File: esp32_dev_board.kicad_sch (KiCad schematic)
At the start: 27 parts, among them J1 USB_B_Micro, J2 Conn_01x12, J3 Conn_01x12, Q1 Q_PMOS_GSD, Q2 MBT3904DW1, SW1 SW_Push, U1 ESP32-WROOM-32, U2 AP2112K-3.3, U3 FT231XS

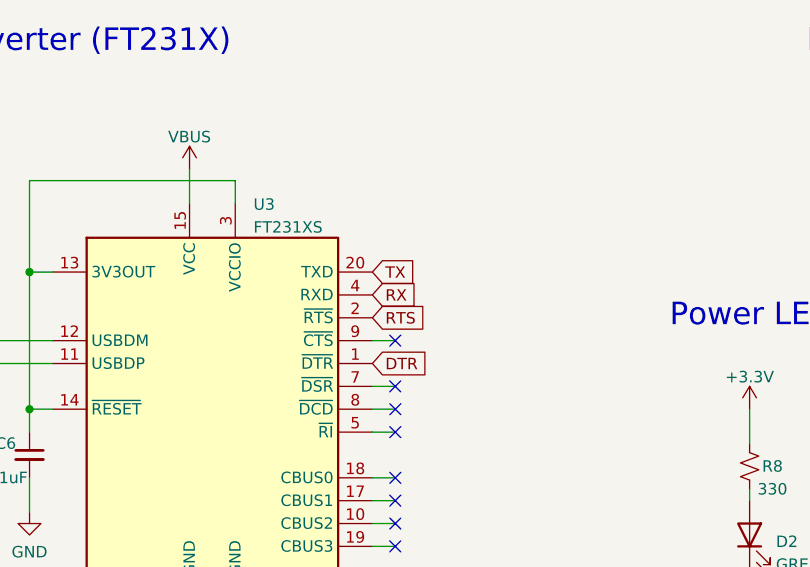
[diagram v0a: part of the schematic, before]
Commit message: Change global labels TX and RX to TX0 and RX0
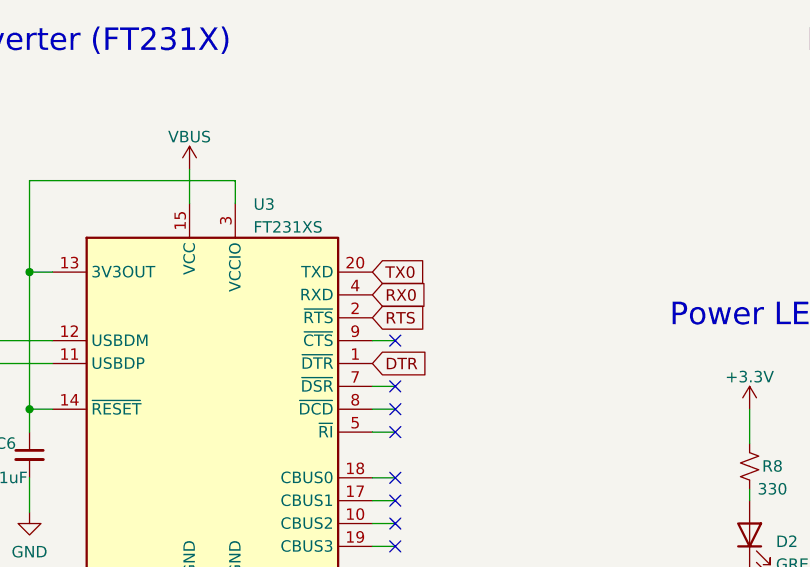
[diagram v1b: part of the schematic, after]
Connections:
- net RX is gone; now on net RX0: U3.4 (RXD)
- net TX is gone; now on net TX0: U3.20 (TXD)
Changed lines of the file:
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@@
     )
   )
-  (global_label "RX" (shape input) (at 181.61 55.88 0) (fields_autoplaced)
+  (global_label "RX0" (shape input) (at 181.61 55.88 0) (fields_autoplaced)
     (effects (font (size 1.27 1.27)) (justify left))
-    (property "Intersheet References" "${INTERSHEET_REFS}" (id 0) (at 186.5026 55.8006 0)
+    (property "Intersheet References" "${INTERSHEET_REFS}" (id 0) (at 187.7121 55.8006 0)
       (effects (font (size 1.27 1.27)) (justify left) hide)
     )
@@
     )
   )
-  (global_label "TX" (shape input) (at 181.61 53.34 0) (fields_autoplaced)
+  (global_label "TX0" (shape input) (at 181.61 53.34 0) (fields_autoplaced)
     (effects (font (size 1.27 1.27)) (justify left))
-    (property "Intersheet References" "${INTERSHEET_REFS}" (id 0) (at 186.2002 53.2606 0)
+    (property "Intersheet References" "${INTERSHEET_REFS}" (id 0) (at 187.4098 53.2606 0)
       (effects (font (size 1.27 1.27)) (justify left) hide)
     )

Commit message: Add silkscreen, round corners, and small fixes
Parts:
- added C7: 1uF, Capacitor_SMD:C_0805_2012Metric_Pad1.18x1.45mm_HandSolder, symbol Device:C_Small
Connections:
- net GND: now also C7.2
- net VIN: now also C7.1
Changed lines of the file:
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@@
   (junction (at 151.13 162.56) (diameter 0) (color 0 0 0 0)
+  )
+  (junction (at 44.45 149.86) (diameter 0) (color 0 0 0 0)
   )
   (no_connect (at 71.12 54.61))
@@
   (no_connect (at 33.02 92.71))
   (no_connect (at 33.02 90.17))
+  (wire (pts (xy 68.58 52.07) (xy 67.31 52.07))
+    (stroke (width 0) (type default) (color 0 0 0 0))
+  )
   (wire (pts (xy 233.68 39.37) (xy 233.68 43.18))
     (stroke (width 0) (type default) (color 0 0 0 0))
@@
     (stroke (width 0) (type default) (color 0 0 0 0))
   )
+  (wire (pts (xy 21.59 176.53) (xy 21.59 180.34))
+    (stroke (width 0) (type default) (color 0 0 0 0))
+  )
   (wire (pts (xy 33.02 85.09) (xy 36.83 85.09))
     (stroke (width 0) (type default) (color 0 0 0 0))
@@
     (stroke (width 0) (type default) (color 0 0 0 0))
   )
-  (wire (pts (xy 29.21 149.86) (xy 29.21 158.75))
+  (wire (pts (xy 29.21 156.21) (xy 29.21 158.75))
     (stroke (width 0) (type default) (color 0 0 0 0))
   )
@@
     (stroke (width 0) (type default) (color 0 0 0 0))
   )
+  (wire (pts (xy 21.59 149.86) (xy 44.45 149.86))
+    (stroke (width 0) (type default) (color 0 0 0 0))
+  )
   (wire (pts (xy 44.45 168.91) (xy 58.42 168.91))
     (stroke (width 0) (type default) (color 0 0 0 0))
@@
     (stroke (width 0) (type default) (color 0 0 0 0))
   )
+  (wire (pts (xy 68.58 49.53) (xy 67.31 49.53))
+    (stroke (width 0) (type default) (color 0 0 0 0))
+  )
   (wire (pts (xy 151.13 172.72) (xy 151.13 162.56))
     (stroke (width 0) (type default) (color 0 0 0 0))
@@
   )
   (wire (pts (xy 138.43 63.5) (xy 146.05 63.5))
+    (stroke (width 0) (type default) (color 0 0 0 0))
+  )
+  (wire (pts (xy 21.59 171.45) (xy 21.59 149.86))
     (stroke (width 0) (type default) (color 0 0 0 0))
   )
@@
     )
   )
-  (global_label "GPIO0" (shape input) (at 67.31 49.53 0) (fields_autoplaced)
-    (effects (font (size 1.27 1.27)) (justify left))
-    (property "Intersheet References" "${INTERSHEET_REFS}" (id 0) (at 75.4079 49.4506 0)
+  (global_label "GPIO0" (shape input) (at 68.58 49.53 0) (fields_autoplaced)
+    (effects (font (size 1.27 1.27)) (justify left))
+    (property "Intersheet References" "${INTERSHEET_REFS}" (id 0) (at 76.6779 49.4506 0)
       (effects (font (size 1.27 1.27)) (justify left) hide)
     )
@@
     )
   )
-  (global_label "TX0" (shape input) (at 67.31 52.07 0) (fields_autoplaced)
-    (effects (font (size 1.27 1.27)) (justify left))
-    (property "Intersheet References" "${INTERSHEET_REFS}" (id 0) (at 73.1098 51.9906 0)
+  (global_label "TX0" (shape input) (at 68.58 52.07 0) (fields_autoplaced)
+    (effects (font (size 1.27 1.27)) (justify left))
+    (property "Intersheet References" "${INTERSHEET_REFS}" (id 0) (at 74.3798 51.9906 0)
       (effects (font (size 1.27 1.27)) (justify left) hide)
     )
@@
     )
     (property "Datasheet" "" (id 3) (at 270.51 156.21 0)
+      (effects (font (size 1.27 1.27)) hide)
+    )
+    (pin "1")
+  )
+  (symbol (lib_id "power:GND") (at 21.59 180.34 0) (unit 1)
+    (in_bom yes) (on_board yes) (fields_autoplaced)
+    (property "Reference" "#PWR024" (id 0) (at 21.59 186.69 0)
+      (effects (font (size 1.27 1.27)) hide)
+    )
+    (property "Value" "GND" (id 1) (at 21.59 184.7834 0))
+    (property "Footprint" "" (id 2) (at 21.59 180.34 0)
+      (effects (font (size 1.27 1.27)) hide)
+    )
+    (property "Datasheet" "" (id 3) (at 21.59 180.34 0)
       (effects (font (size 1.27 1.27)) hide)
     )
@@
     (pin "2")
   )
+  (symbol (lib_id "Device:C_Small") (at 21.59 173.99 0) (unit 1)
+    (in_bom yes) (on_board yes)
+    (property "Reference" "C7" (id 0) (at 16.51 175.26 0)
+      (effects (font (size 1.27 1.27)) (justify left))
+    )
+    (property "Value" "1uF" (id 1) (at 16.51 177.8 0)
+      (effects (font (size 1.27 1.27)) (justify left))
+    )
+    (property "Footprint" "Capacitor_SMD:C_0805_2012Metric_Pad1.18x1.45mm_HandSolder" (id 2) (at 21.59 173.99 0)
+      (effects (font (size 1.27 1.27)) hide)
+    )
+    (property "Datasheet" "~" (id 3) (at 21.59 173.99 0)
+      (effects (font (size 1.27 1.27)) hide)
+    )
+    (pin "1")
+    (pin "2")
+  )
   (symbol (lib_id "power:GND") (at 66.04 180.34 0) (unit 1)
     (in_bom yes) (on_board yes) (fields_autoplaced)
@@
     (pin "1")
   )
-  (symbol (lib_id "power:VBUS") (at 29.21 149.86 0) (unit 1)
-    (in_bom yes) (on_board yes) (fields_autoplaced)
-    (property "Reference" "#PWR01" (id 0) (at 29.21 153.67 0)
-      (effects (font (size 1.27 1.27)) hide)
-    )
-    (property "Value" "VBUS" (id 1) (at 29.21 146.2842 0))
-    (property "Footprint" "" (id 2) (at 29.21 149.86 0)
-      (effects (font (size 1.27 1.27)) hide)
-    )
-    (property "Datasheet" "" (id 3) (at 29.21 149.86 0)
+  (symbol (lib_id "power:VBUS") (at 29.21 156.21 0) (unit 1)
+    (in_bom yes) (on_board yes)
+    (property "Reference" "#PWR01" (id 0) (at 29.21 160.02 0)
+      (effects (font (size 1.27 1.27)) hide)
+    )
+    (property "Value" "VBUS" (id 1) (at 29.21 152.4 0))
+    (property "Footprint" "" (id 2) (at 29.21 156.21 0)
+      (effects (font (size 1.27 1.27)) hide)
+    )
+    (property "Datasheet" "" (id 3) (at 29.21 156.21 0)
       (effects (font (size 1.27 1.27)) hide)
     )
@@
       (reference "#PWR023") (unit 1) (value "GND") (footprint "")
     )
+    (path "/43dd37ed-ec03-48c6-b286-66c81e1fab72"
+      (reference "#PWR024") (unit 1) (value "GND") (footprint "")
+    )
     (path "/3f4b71e4-2445-4d0d-b154-9c9af62cd76e"
       (reference "C1") (unit 1) (value "1uF") (footprint "Capacitor_SMD:C_0805_2012Metric_Pad1.18x1.45mm_HandSolder")
@@
       (reference "C6") (unit 1) (value "0.1uF") (footprint "Capacitor_SMD:C_0805_2012Metric_Pad1.18x1.45mm_HandSolder")
     )
+    (path "/60a0fca1-9286-4820-ae51-67d1b248f51e"
+      (reference "C7") (unit 1) (value "1uF") (footprint "Capacitor_SMD:C_0805_2012Metric_Pad1.18x1.45mm_HandSolder")
+    )
     (path "/a979677f-6ca5-4860-bd71-7214e30244d3"

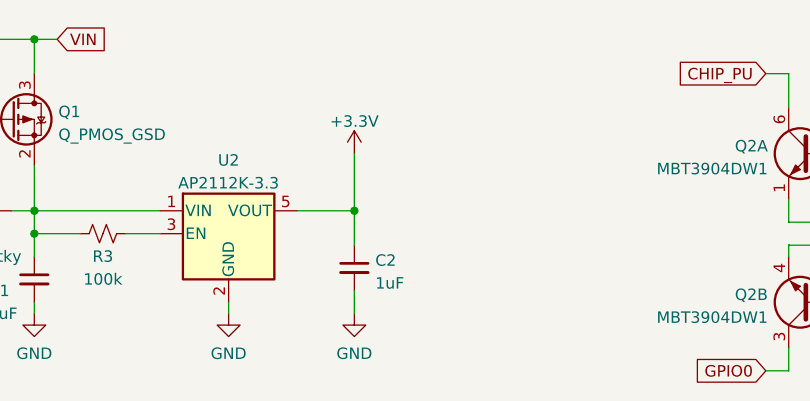
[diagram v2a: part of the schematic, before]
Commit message: Change C2 value and add back silkscreen
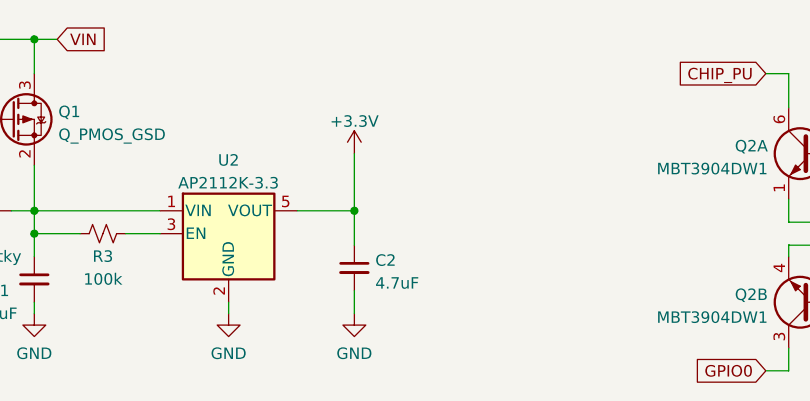
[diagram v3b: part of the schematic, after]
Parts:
- C2: value 1uF -> 4.7uF
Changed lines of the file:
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@@
       (effects (font (size 1.27 1.27)) (justify left))
     )
-    (property "Value" "1uF" (id 1) (at 82.3341 176.9685 0)
+    (property "Value" "4.7uF" (id 1) (at 82.3341 176.9685 0)
       (effects (font (size 1.27 1.27)) (justify left))
     )
@@
     )
     (path "/eb8e7f55-f965-4a34-94e5-32545086e3d6"
-      (reference "C2") (unit 1) (value "1uF") (footprint "Capacitor_SMD:C_0805_2012Metric_Pad1.18x1.45mm_HandSolder")
+      (reference "C2") (unit 1) (value "4.7uF") (footprint "Capacitor_SMD:C_0805_2012Metric_Pad1.18x1.45mm_HandSolder")
     )
     (path "/5467467e-0542-42da-902e-a472b0e9d541"

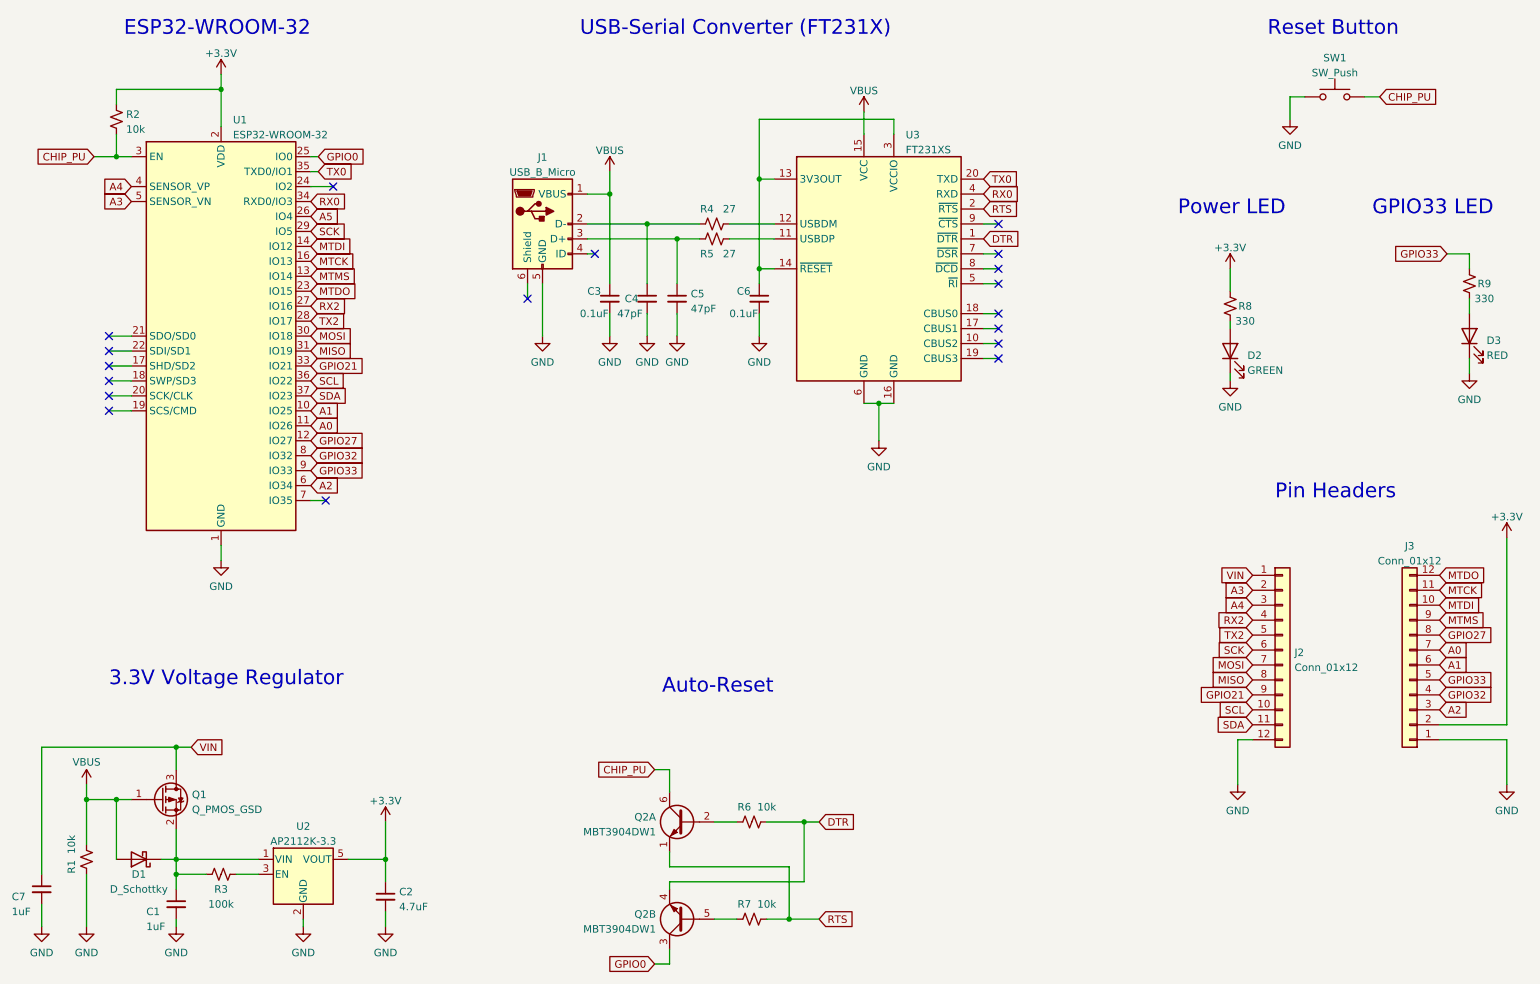
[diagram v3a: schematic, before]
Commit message: Fix serial connection between ESP32 and FT231X
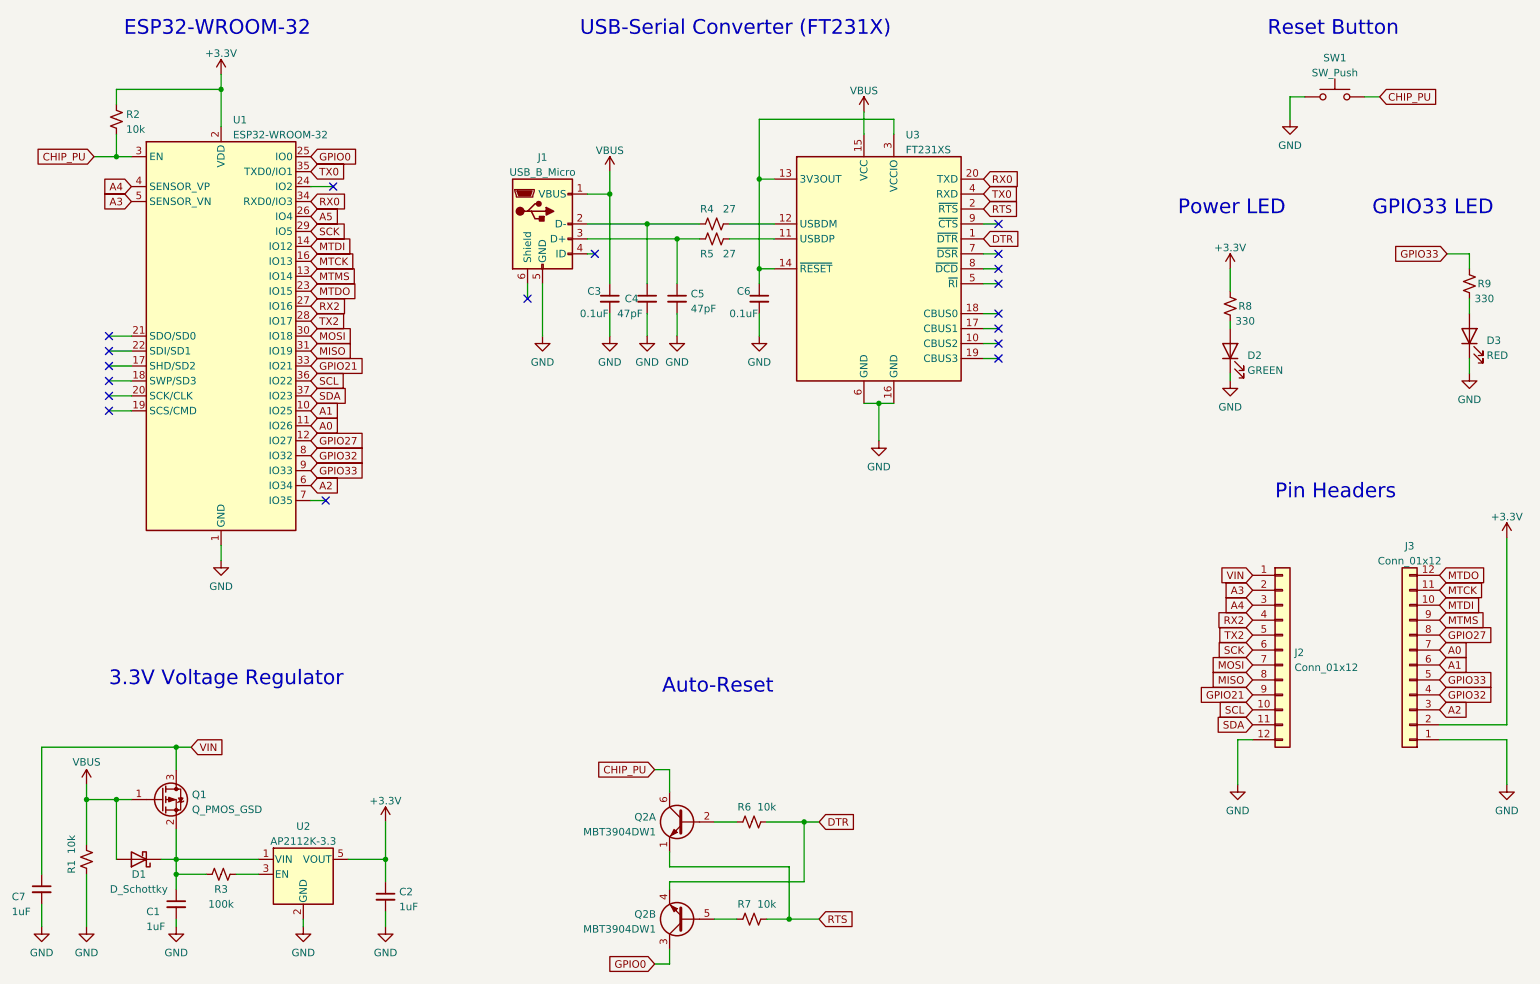
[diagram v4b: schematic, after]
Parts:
- C2: value 4.7uF -> 1uF
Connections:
- net RX0: now also U3.20 (TXD); no longer U3.4 (RXD)
- net TX0: now also U3.4 (RXD); no longer U3.20 (TXD)
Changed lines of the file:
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@@
   (no_connect (at 33.02 92.71))
   (no_connect (at 33.02 90.17))
-  (wire (pts (xy 68.58 52.07) (xy 67.31 52.07))
-    (stroke (width 0) (type default) (color 0 0 0 0))
-  )
   (wire (pts (xy 233.68 39.37) (xy 233.68 43.18))
     (stroke (width 0) (type default) (color 0 0 0 0))
@@
   )
   (wire (pts (xy 259.08 146.05) (xy 270.51 146.05))
-    (stroke (width 0) (type default) (color 0 0 0 0))
-  )
-  (wire (pts (xy 68.58 49.53) (xy 67.31 49.53))
     (stroke (width 0) (type default) (color 0 0 0 0))
   )
@@
     )
   )
-  (global_label "GPIO0" (shape input) (at 68.58 49.53 0) (fields_autoplaced)
-    (effects (font (size 1.27 1.27)) (justify left))
-    (property "Intersheet References" "${INTERSHEET_REFS}" (id 0) (at 76.6779 49.4506 0)
+  (global_label "GPIO0" (shape input) (at 67.31 49.53 0) (fields_autoplaced)
+    (effects (font (size 1.27 1.27)) (justify left))
+    (property "Intersheet References" "${INTERSHEET_REFS}" (id 0) (at 75.4079 49.4506 0)
       (effects (font (size 1.27 1.27)) (justify left) hide)
     )
@@
     )
   )
-  (global_label "RX0" (shape input) (at 181.61 55.88 0) (fields_autoplaced)
-    (effects (font (size 1.27 1.27)) (justify left))
-    (property "Intersheet References" "${INTERSHEET_REFS}" (id 0) (at 187.7121 55.8006 0)
+  (global_label "RX0" (shape input) (at 181.61 53.34 0) (fields_autoplaced)
+    (effects (font (size 1.27 1.27)) (justify left))
+    (property "Intersheet References" "${INTERSHEET_REFS}" (id 0) (at 187.7121 53.2606 0)
       (effects (font (size 1.27 1.27)) (justify left) hide)
     )
@@
     )
   )
-  (global_label "TX0" (shape input) (at 181.61 53.34 0) (fields_autoplaced)
-    (effects (font (size 1.27 1.27)) (justify left))
-    (property "Intersheet References" "${INTERSHEET_REFS}" (id 0) (at 187.4098 53.2606 0)
-      (effects (font (size 1.27 1.27)) (justify left) hide)
-    )
-  )
-  (global_label "TX0" (shape input) (at 68.58 52.07 0) (fields_autoplaced)
-    (effects (font (size 1.27 1.27)) (justify left))
-    (property "Intersheet References" "${INTERSHEET_REFS}" (id 0) (at 74.3798 51.9906 0)
+  (global_label "TX0" (shape input) (at 181.61 55.88 0) (fields_autoplaced)
+    (effects (font (size 1.27 1.27)) (justify left))
+    (property "Intersheet References" "${INTERSHEET_REFS}" (id 0) (at 187.4098 55.8006 0)
+      (effects (font (size 1.27 1.27)) (justify left) hide)
+    )
+  )
+  (global_label "TX0" (shape input) (at 67.31 52.07 0) (fields_autoplaced)
+    (effects (font (size 1.27 1.27)) (justify left))
+    (property "Intersheet References" "${INTERSHEET_REFS}" (id 0) (at 73.1098 51.9906 0)
       (effects (font (size 1.27 1.27)) (justify left) hide)
     )
@@
       (effects (font (size 1.27 1.27)) (justify left))
     )
-    (property "Value" "4.7uF" (id 1) (at 82.3341 176.9685 0)
+    (property "Value" "1uF" (id 1) (at 82.3341 176.9685 0)
       (effects (font (size 1.27 1.27)) (justify left))
     )
@@
     )
     (path "/eb8e7f55-f965-4a34-94e5-32545086e3d6"
-      (reference "C2") (unit 1) (value "4.7uF") (footprint "Capacitor_SMD:C_0805_2012Metric_Pad1.18x1.45mm_HandSolder")
+      (reference "C2") (unit 1) (value "1uF") (footprint "Capacitor_SMD:C_0805_2012Metric_Pad1.18x1.45mm_HandSolder")
     )
     (path "/5467467e-0542-42da-902e-a472b0e9d541"
